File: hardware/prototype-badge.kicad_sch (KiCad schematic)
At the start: 31 parts, among them J1 GCT4105, SW1 BOOTSEL, SW2 RESET, U1 USBLC6-2SC6, U2 AMS1117-3.3, U3 W25Q32JVSS, U4 RP2040, Y1 12MHz

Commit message: started pcb
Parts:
- added C17, C19: 4.7uF, Capacitor_SMD:C_0603_1608Metric, symbol Device:C_Small
- added C18, C20, C21, C22, C23, C24, C25, C26, C28: 1uF, Capacitor_SMD:C_0603_1608Metric, symbol Device:C_Small
- added C27: 220nF, Capacitor_SMD:C_0402_1005Metric, symbol Device:C_Small
- added C29: 100nF, Capacitor_SMD:C_0402_1005Metric, symbol Device:C_Small
- added D1, D2, D3: MBR0530, Diode_SMD:D_SOD-123, symbol Diode:MBR0530
- added D4: LED_Small, LED_SMD:LED_0603_1608Metric, symbol Device:LED_Small
- added D5: D_Photo, OptoDevice:Kingbright_KPS-3227, symbol Device:D_Photo
- added J2: E-Ink, Connector_FFC-FPC:TE_2-1734839-4_1x24-1MP_P0.5mm_Horizontal, symbol Connector_Generic_MountingPin:Conn_01x24_MountingPin
- added L1: 10uH, Inductor_SMD:L_APV_ANR4018, symbol Device:L_Small
- added Q1: Si1308EDL, Package_TO_SOT_SMD:SOT-323_SC-70, symbol Transistor_FET:Si1308EDL
- added R12: 47R, Resistor_SMD:R_0603_1608Metric, symbol Device:R_Small_US
- added R13, R14: 10kR, Resistor_SMD:R_0402_1005Metric, symbol Device:R_Small_US
- added R15: 220kR, Resistor_SMD:R_0603_1608Metric, symbol Device:R_Small_US
- added R8: 1MR, Resistor_SMD:R_0603_1608Metric, symbol Device:R_Small_US
- added R9: 2.2R, Resistor_SMD:R_0603_1608Metric, symbol Device:R_Small_US
- added SW3: User1, Button_Switch_SMD:SW_Tactile_SPST_NO_Straight_CK_PTS636Sx25SMTRLFS, symbol Switch:SW_Push
- added SW4: User2, Button_Switch_SMD:SW_Tactile_SPST_NO_Straight_CK_PTS636Sx25SMTRLFS, symbol Switch:SW_Push
- added SW5: User3, Button_Switch_SMD:SW_Tactile_SPST_NO_Straight_CK_PTS636Sx25SMTRLFS, symbol Switch:SW_Push
- added SW6: User4, Button_Switch_SMD:SW_Tactile_SPST_NO_Straight_CK_PTS636Sx25SMTRLFS, symbol Switch:SW_Push
- added SW7: LIGHTPROG, Button_Switch_SMD:SW_Tactile_SPST_NO_Straight_CK_PTS636Sx25SMTRLFS, symbol Switch:SW_Push
- added U5: NT3H2111-2211, footprints:NT3H2111W0FHKH, symbol prototype-badge:NT3H2111_2211
- added U6: LMV321, Package_TO_SOT_SMD:SOT-23-5, symbol Amplifier_Operational:LMV321
- C10, C11, C12, C13, C14, C15, C16, C3, C6, C7: footprint (none) -> Capacitor_SMD:C_0402_1005Metric; LCSC (none) -> C1525
- C4, C5: value ? -> 12pF; footprint (none) -> Capacitor_SMD:C_0402_1005Metric; LCSC (none) -> C1547
- C8, C9: footprint (none) -> Capacitor_SMD:C_0603_1608Metric; LCSC (none) -> C15849
- R1, R2: footprint (none) -> Resistor_SMD:R_0402_1005Metric; LCSC (none) -> C25905
- R3: footprint (none) -> Resistor_SMD:R_0402_1005Metric; LCSC (none) -> C25744
- R4, R5: footprint (none) -> Resistor_SMD:R_0402_1005Metric; LCSC (none) -> C274349
- R6, R7: footprint (none) -> Resistor_SMD:R_0402_1005Metric; LCSC (none) -> C11702
- SW1, SW2: footprint (none) -> Button_Switch_SMD:SW_Tactile_SPST_NO_Straight_CK_PTS636Sx25SMTRLFS; LCSC (none) -> C318938
- U3: LCSC (none) -> C97521
- U4: LCSC (none) -> C2040
- Y1: LCSC (none) -> C37635368
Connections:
- net +3.3V: now also C19.1, C20.2, C28.1, J2.10 (Pin_10), J2.9 (Pin_9), L1.1, R13.1, U5.6 (VDD), U6.5 (V+)
- net Earth: now also C18.2, C19.2, C20.1, C21.1, C22.1, C23.1, C24.1, C25.1, C26.2, C27.2, C28.2, C29.1, D2.1 (K), D4.1 (K), D5.2 (A), J2.17 (Pin_17), J2.8 (Pin_8), J2.MP (MountPin), R14.2, R8.1, R9.2, SW3.2, SW4.2, SW5.2, SW6.2, SW7.2, U5.2 (VSS), U6.2 (V-)
- net GPIO13: now also SW7.1
- net GPIO14: now also SW3.1
- net GPIO15: now also SW4.1
- net GPIO16: now also SW5.1
- net GPIO17: now also SW6.1
- net GPIO0 renamed I2C_SDA
- net I2C_SDA: now also U5.5 (SDA)
- net GPIO1 renamed I2C_SCL
- net I2C_SCL: now also U5.3 (SCL)
- net GPIO18 renamed SPI_CLK
- net SPI_CLK: now also J2.12 (Pin_12)
- net GPIO19 renamed SPI_MOSI
- net SPI_MOSI: now also J2.11 (Pin_11)
- net GPIO24 renamed DISP_CS
- net DISP_CS: now also J2.13 (Pin_13)
- net GPIO25 renamed DISP_DC
- net DISP_DC: now also J2.14 (Pin_14)
- net GPIO26_ADC0 renamed DISP_RST
- net DISP_RST: now also J2.15 (Pin_15)
- net GPIO27_ADC1 renamed DISP_BUSY
- net DISP_BUSY: now also J2.16 (Pin_16)
- net GPIO28_ADC2 renamed GPIO28_ADC2_LDR
- net GPIO28_ADC2_LDR: now also R15.1, U6.4
- new net: C26.1, J2.1 (Pin_1)
- new net: C29.2, R13.2, R14.1, U6.1 (+)
- new net: D5.1 (K), R15.2, U6.3 (-)
- new net: C27.1, R12.1, U5.7 (VOUT)
- new net: D4.2 (A), R12.2
- new net: C17.2, D3.2 (A), L1.2, Q1.3 (D)
- new net: C23.2, J2.5 (Pin_5)
- new net: U5.1 (LA), U5.8 (LB)
- new net: C17.1, D1.1 (K), D2.2 (A)
- new net: C21.2, J2.20 (Pin_20)
- new net: C24.2, J2.3 (Pin_3)
- new net: C22.2, J2.7 (Pin_7)
- new net DISP_GDR: J2.23 (Pin_23), Q1.1 (G), R8.2
- new net DISP_PREVGH: C18.1, D3.1 (K), J2.4 (Pin_4)
- new net DISP_PREVGL: C25.2, D1.2 (A), J2.2 (Pin_2)
- new net DISP_RESE: J2.22 (Pin_22), Q1.2 (S), R9.1
- no-connect marks 5 -> 11
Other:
- note added: "---FLIPPED PINS FOR TOP MOUNT---"
- note added: "E-Ink Display - 2.9""
- note added: "NFC Tag"
- note added: "Photodiode"
- note added: "Press to activate light programming"
- note added: "RP2040 MCU"
- note added: "USB Input"
- note added: "User-Facing Buttons"
- note added: "config over light?"
- note added: "overcomplicated TIA circuit"
- title: (none) -> Prototype PCB Badges
- moved on the sheet: C1, C10, C11, C12, C13, C14, C15, C16, C2, C3, C4, C5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

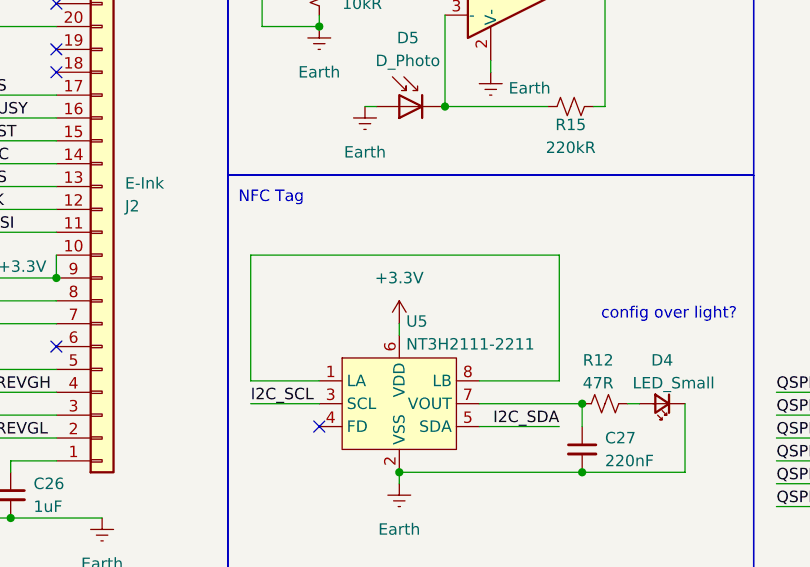
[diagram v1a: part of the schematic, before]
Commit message: 90% done with pcb, need to add dev pins
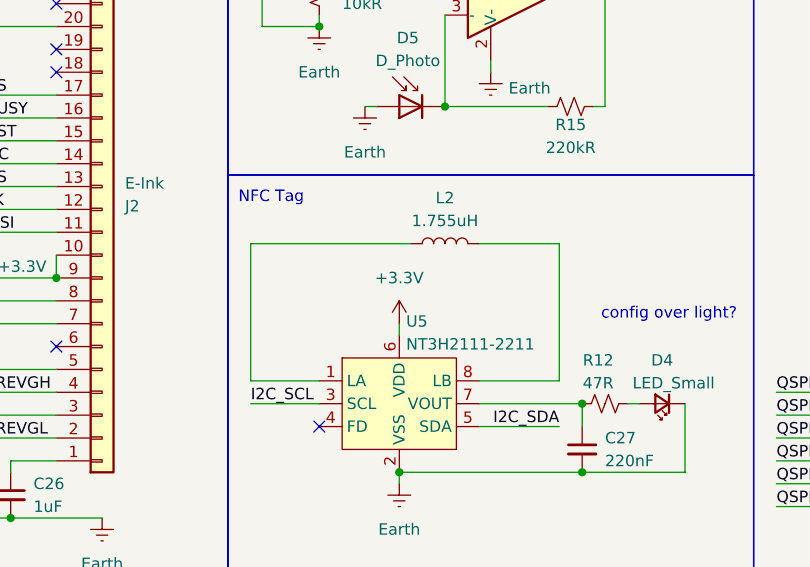
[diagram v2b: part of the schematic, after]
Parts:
- added L2: 1.755uH, footprints:nfc-coil-2, symbol Device:L
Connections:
- net at U5.1 (LA): now also L2.1; no longer U5.8 (LB)
- new net: L2.2, U5.8 (LB)
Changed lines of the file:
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@@
 	(wire
 		(pts
+			(xy 148.59 120.65) (xy 148.59 135.89)
+		)
+		(stroke
+			(width 0)
+			(type default)
+		)
+	)
+	(wire
+		(pts
 			(xy 226.06 156.21) (xy 224.79 156.21)
 		)
@@
 	(wire
 		(pts
-			(xy 148.59 135.89) (xy 148.59 121.92)
+			(xy 193.04 130.81) (xy 193.04 132.08)
 		)
 		(stroke
@@
 	(wire
 		(pts
-			(xy 193.04 130.81) (xy 193.04 132.08)
+			(xy 182.88 50.8) (xy 191.77 50.8)
 		)
 		(stroke
@@
 	(wire
 		(pts
-			(xy 182.88 50.8) (xy 191.77 50.8)
+			(xy 148.59 120.65) (xy 139.7 120.65)
 		)
 		(stroke
@@
 	(wire
 		(pts
-			(xy 114.3 121.92) (xy 114.3 135.89)
+			(xy 44.45 40.64) (xy 44.45 43.18)
 		)
 		(stroke
@@
 	(wire
 		(pts
-			(xy 44.45 40.64) (xy 44.45 43.18)
+			(xy 193.04 158.75) (xy 193.04 157.48)
 		)
 		(stroke
@@
 	(wire
 		(pts
-			(xy 193.04 158.75) (xy 193.04 157.48)
+			(xy 148.59 35.56) (xy 148.59 45.72)
 		)
 		(stroke
@@
 	(wire
 		(pts
-			(xy 148.59 35.56) (xy 148.59 45.72)
+			(xy 191.77 36.83) (xy 191.77 38.1)
 		)
 		(stroke
@@
 	(wire
 		(pts
-			(xy 191.77 36.83) (xy 191.77 38.1)
+			(xy 248.92 116.84) (xy 270.51 116.84)
 		)
 		(stroke
@@
 	(wire
 		(pts
-			(xy 248.92 116.84) (xy 270.51 116.84)
+			(xy 232.41 149.86) (xy 229.87 149.86)
 		)
 		(stroke
@@
 	(wire
 		(pts
-			(xy 232.41 149.86) (xy 229.87 149.86)
+			(xy 114.3 120.65) (xy 114.3 135.89)
 		)
 		(stroke
@@
 	(wire
 		(pts
-			(xy 191.77 43.18) (xy 198.12 43.18)
+			(xy 132.08 120.65) (xy 114.3 120.65)
 		)
 		(stroke
@@
 	(wire
 		(pts
-			(xy 39.37 142.24) (xy 39.37 130.81)
+			(xy 191.77 43.18) (xy 198.12 43.18)
 		)
 		(stroke
@@
 	(wire
 		(pts
-			(xy 80.01 88.9) (xy 92.71 88.9)
+			(xy 39.37 142.24) (xy 39.37 130.81)
 		)
 		(stroke
@@
 	(wire
 		(pts
-			(xy 130.81 147.32) (xy 130.81 146.05)
+			(xy 80.01 88.9) (xy 92.71 88.9)
 		)
 		(stroke
@@
 	(wire
 		(pts
-			(xy 266.7 53.34) (xy 248.92 53.34)
+			(xy 130.81 147.32) (xy 130.81 146.05)
 		)
 		(stroke
@@
 	(wire
 		(pts
-			(xy 80.01 111.76) (xy 92.71 111.76)
+			(xy 266.7 53.34) (xy 248.92 53.34)
 		)
 		(stroke
@@
 	(wire
 		(pts
-			(xy 148.59 121.92) (xy 114.3 121.92)
+			(xy 80.01 111.76) (xy 92.71 111.76)
 		)
 		(stroke
@@
 			"hBBCCCGEEEIIIYQQQgghhBBCCCGEEEIIIYQQQgghhBBCCCGEEEIIIYQQQgghhBBCCCGEEEIIIYQQ"
 			"QgghhBBCCCGEEEIIIYQQQgghhBBCCCGEEEIIIYQQQgghhBBCCCGEEEIIIYQQQhai/w/KaxpFstuM"
-			"6gAAAABJRU5ErkJggg=="
+			"6gAAAABJRU5ErkJgggAAAAAAAAAAAAAAAAAAAAAAAAAAAAAAAAAAAAAAAAAAAAAAAAAAAAAAAAAA"
+			"AAAAAAAAAAAAAAAAAAAAAAAAAAAAAAAAAAAAAAAAAAAAAAAAAAAAAAAAAAAAAAAAAAAAAAAAAAAA"
+			"AAAAAAAAAAAAAAAAAAAAAAAAAAAAAAAAAAAAAAAAAAAAAAAAAAAAAAAAAAAAAAAAAAAAAAAAAAAA"
+			"AAAAAAAAAAAAAAAAAAAAAAAAAAAAAAAAAAAAAAAAAAAAAAAAAAAAAAAAAAAAAAAAAAAAAAAAAAAA"
+			"AAAAAAAAAAAAAAAAAAAAAAAAAAAAAAAAAAAAAAAAAAAAAAAAAAAAAAAAAAAAAAAAAAAAAAAAAAAA"
+			"AAAAAAAAAAAAAAAAAAAAAAAAAAAAAAAAAAAAAAAAAAAAAAAAAAAAAAAAAAAAAAAAAAAAAAAAAAAA"
+			"AAAAAAAAAAAAAAAAAAAAAAAAAAAAAAAAAAAAAAAAAAAAAAAAAAAAAAAAAAAAAAAAAAAAAAAAAAAA"
+			"AAAAAAAAAAAAAAAAAAAAAAAAAAAAAAAAAAAAAAAAAAAAAAAAAAAAAAAAAAAAAAAAAAAAAAAAAAAA"
+			"AAAAAAAAAAAAAAAAAAAAAAAAAAAAAAAAAAAAAAAAAAAAAAAAAAAAAAAAAAAAAAAAAAAAAAAAAAAA"
+			"AAAAAAAAAAAAAAAAAAAAAAAAAAAAAAAAAAAAAAAAAAAAAAAAAAAAAAAAAAAAAAAAAAAAAAAAAAAA"
+			"AAAAAAAAAAAAAAAAAAAAAAAAAAAAAAAAAAAAAAAAAAAAAAAAAAAAAAAAAAAAAAAAAAAAAAAAAAAA"
+			"AAAAAAAAAAAAAAAAAAAAAAAAAAAAAAAAAAAAAAAAAAAAAAAAAAAAAAAAAAAAAAAAAAAAAAAAAAAA"
+			"AAAAAAAAAAAAAAAAAAAAAAAAAAAAAAAAAAAAAAAAAAAAAAAAAAAAAAAAAAAAAAAAAAAAAAAAAAAA"
+			"AAAAAAAAAAAAAAAAAAAAAAAAAAAAAAAAAAAAAAAAAAAAAAAAAAAAAAAAAAAAAAAAAAAAAAAAAAAA"
+			"AAAAAAAAAAAAAAAAAAAAAAAAAAAAAAAAAAAAAAAAAAAAAAAAAAAAAAAAAAAAAAAAAAAAAAAAAAAA"
+			"AAAAAAAAAAAAAAAAAAAAAAAAAAAAAAAAAAAAAAAAAAAAAAAAAAAAAAAAAAAAAAAAAAAAAAAAAAAA"
+			"AAAAAAAAAAAAAAAAAAAAAAAAAAAAAAAAAAAAAAAAAAAAAAAAAAAAAAAAAAAAAAAAAAAAAAAAAAAA"
+			"AAAAAAAAAAAAAAAAAAAAAAAAAAAAAAAAAAAAAAAAAAAAAAAAAAAAAAAAAAAAAAAAAAAAAAAAAAAA"
+			"AAAAAAAAAAAAAAAAAAAAAAAAAAAAAAAAAAAAAAAAAAAAAAAAAAAAAAAAAAAAAAAAAAAAAAAAAAAA"
+			"AAAAAAAAAAAAAAAAAAAAAAAAAAAAAAAAAAAAAAAAAAAAAAAAAAAAAAAAAAAAAAAAAAAAAAAAAAAA"
+			"AAAAAAAAAAAAAAAAAAAAAAAAAAAAAAAAAAAAAAAAAAAAAAAAAAAAAAAAAAAAAAAAAAAAAAAAAAAA"
+			"AAAAAAAAAAAAAAAAAAAAAAAAAAAAAAAAAAAAAAAAAAAAAAAAAAAAAAAAAAAAAAAAAAAAAAAAAAAA"
+			"AAAAAAAAAAAAAAAAAAAAAAAAAAAAAAAAAAAAAAAAAAAAAAAAAAAAAAAAAAAAAAAAAAAAAAAAAAAA"
+			"AAAAAAAAAAAAAAAAAAAAAAAAAAAAAAAAAAAAAAAAAAAAAAAAAAAAAAAAAAAAAAAAAAAAAAAAAAAA"
+			"AAAAAAAAAAAAAAAAAAAAAAAAAAAAAAAAAAAAAAAAAAAAAAAAAAAAAAAAAAAAAAAAAAAAAAAAAAAA"
+			"AAAAAAAAAAAAAAAAAAAAAAAAAAAAAAAAAAAAAAAAAAAAAAAAAAAAAAAAAAAAAAAAAAAAAAAAAAAA"
+			"AAAAAAAAAAAAAAAAAAAAAAAAAAAAAAAAAAAAAAAAAAAAAAAAAAAAAAAAAAAAAAAAAAAAAAAAAAAA"
+			"AAAAAAAAAAAAAAAAAAAAAAAAAAAAAAAAAAAAAAAAAAAAAAAAAAAAAAAAAAAAAAAAAAAAAAAAAAAA"
+			"AAAAAAAAAAAAAAAAAAAAAAAAAAAAAAAAAAAAAAAAAAAAAAAAAAAAAAAAAAAAAAAAAAAAAAAAAAAA"
+			"AAAAAAAAAAAAAAAAAAAAAAAAAAAAAAAAAAAAAAAAAAAAAAAAAAAAAAAAAAAAAAAAAAAAAAAAAAAA"
+			"AAAAAAAAAAAAAAAAAAAAAAAAAAAAAAAAAAAAAAAAAAAAAAAAAAAAAAAAAAAAAAAAAAAAAAAAAAAA"
+			"AAAAAAAAAAAAAAAAAAAAAAAAAAAAAAAAAAAAAAAAAAAAAAAAAAAAAAAAAAAAAAAAAAAAAAAAAAAA"
+			"AAAAAAAAAAAAAAAAAAAAAAAAAAAAAAAAAAAAAAAAAAAAAAAAAAAAAAAAAAAAAAAAAAAAAAAAAAAA"
+			"AAAAAAAAAAAAAAAAAAAAAAAAAAAAAAAAAAAAAAAAAAAAAAAAAAAAAAAAAAAAAAAAAAAAAAAAAAAA"
+			"AAAAAAAAAAAAAAAAAAAAAAAAAAAAAAAAAAAAAAAAAAAAAAAAAAAAAAAAAAAAAAAAAAAAAAAAAAAA"
+			"AAAAAAAAAAAAAAAAAAAAAAAAAAAAAAAAAAAAAAAAAAAAAAAAAAAAAAAAAAAAAAAAAAAAAAAAAAAA"
+			"AAAAAAAAAAAAAAAAAA=="
 		)
 	)
@@
 			"K8ZsyVreCyWJuaoBAAAAAAAAAAAAAAAAAAAAAAAAAAAAAAAAAAAAAAAAAAAAAAAAAAAAAAAAAAAA"
 			"AAAAAAAAAAAAAAAAAAAAAAAAAAAAAAAAAAAAAAAAAAAAAAAAAAAAAAAAAAAAAACwOv0fB0wq9b7e"
-			"qgAAAAAASUVORK5CYII="
+			"qgAAAAAASUVORK5CYIIAAAAAAAAAAAAAAAAAAAAAAAAAAAAAAAAAAAAAAAAAAAAAAAAAAAAAAAAA"
+			"AAAAAAAAAAAAAAAAAAAAAAAAAAAAAAAAAAAAAAAAAAAAAAAAAAAAAAAAAAAAAAAAAAAAAAAAAAAA"
+			"AAAAAAAAAAAAAAAAAAAAAAAAAAAAAAAAAAAAAAAAAAAAAAAAAAAAAAAAAAAAAAAAAAAAAAAAAAAA"
+			"AAAAAAAAAAAAAAAAAAAAAAAAAAAAAAAAAAAAAAAAAAAAAAAAAAAAAAAAAAAAAAAAAAAAAAAAAAAA"
+			"AAAAAAAAAAAAAAAAAAAAAAAAAAAAAAAAAAAAAAAAAAAAAAAAAAAAAAAAAAAAAAAAAAAAAAAAAAAA"
+			"AAAAAAAAAAAAAAAAAAAAAAAAAAAAAAAAAAAAAAAAAAAAAAAAAAAAAAAAAAAAAAAAAAAAAAAAAAAA"
+			"AAAAAAAAAAAAAAAAAAAAAAAAAAAAAAAAAAAAAAAAAAAAAAAAAAAAAAAAAAAAAAAAAAAAAAAAAAAA"
+			"AAAAAAAAAAAAAAAAAAAAAAAAAAAAAAAAAAAAAAAAAAAAAAAAAAAAAAAAAAAAAAAAAAAAAAAAAAAA"
+			"AAAAAAAAAAAAAAAAAAAAAAAAAAAAAAAAAAAAAAAAAAAAAAAAAAAAAAAAAAAAAAAAAAAAAAAAAAAA"
+			"AAAAAAAAAAAAAAAAAAAAAAAAAAAAAAAAAAAAAAAAAAAAAAAAAAAAAAAAAAAAAAAAAAAAAAAAAAAA"
+			"AAAAAAAAAAAAAAAAAAAAAAAAAAAAAAAAAAAAAAAAAAAAAAAAAAAAAAAAAAAAAAAAAAAAAAAAAAAA"
+			"AAAAAAAAAAAAAAAAAAAAAAAAAAAAAAAAAAAAAAAAAAAAAAAAAAAAAAAAAAAAAAAAAAAAAAAAAAAA"
+			"AAAAAAAAAAAAAAAAAAAAAAAAAAAAAAAAAAAAAAAAAAAAAAAAAAAAAAAAAAAAAAAAAAAAAAAAAAAA"
+			"AAAAAAAAAAAAAAAAAAAAAAAAAAAAAAAAAAAAAAAAAAAAAAAAAAAAAAAAAAAAAAAAAAAAAAAAAAAA"
+			"AAAAAAAAAAAAAAAAAAAAAAAAAAAAAAAAAAAAAAAAAAAAAAAAAAAAAAAAAAAAAAAAAAAAAAAAAAAA"
+			"AAAAAAAAAAAAAAAAAAAAAAAAAAAAAAAAAAAAAAAAAAAAAAAAAAAAAAAAAAAAAAAAAAAAAAAAAAAA"
+			"AAAAAAAAAAAAAAAAAAAAAAAAAAAAAAAAAAAAAAAAAAAAAAAAAAAAAAAAAAAAAAAAAAAAAAAAAAAA"
+			"AAAAAAAAAAAAAAAAAAAAAAAAAAAAAAAAAAAAAAAAAAAAAAAAAAAAAAAAAAAAAAAAAAAAAAAAAAAA"
+			"AAAAAAAAAAAAAAAAAAAAAAAAAAAAAAAAAAAAAAAAAAAAAAAAAAAAAAAAAAAAAAAAAAAAAAAAAAAA"
+			"AAAAAAAAAAAAAAAAAAAAAAAAAAAAAAAAAAAAAAAAAAAAAAAAAAAAAAAAAAAAAAAAAAAAAAAAAAAA"
+			"AAAAAAAAAAAAAAAAAAAAAAAAAAAAAAAAAAAAAAAAAAAAAAAAAAAAAAAAAAAAAAAAAAAAAAAAAAAA"
+			"AAAAAAAAAAAAAAAAAAAAAAAAAAAAAAAAAAAAAAAAAAAAAAAAAAAAAAAAAAAAAAAAAAAAAAAAAAAA"
+			"AAAAAAAAAAAAAAAAAAAAAAAAAAAAAAAAAAAAAAAAAAAAAAAAAAAAAAAAAAAAAAAAAAAAAAAAAAAA"
+			"AAAAAAAAAAAAAAAAAAAAAAAAAAAAAAAAAAAAAAAAAAAAAAAAAAAAAAAAAAAAAAAAAAAAAAAAAAAA"
+			"AAAAAAAAAAAAAAAAAAAAAAAAAAAAAAAAAAAAAAAAAAAAAAAAAAAAAAAAAAAAAAAAAAAAAAAAAAAA"
+			"AAAAAAAAAAAAAAAAAAAAAAAAAAAAAAAAAAAAAAAAAAAAAAAAAAAAAAAAAAAAAAAAAAAAAAAAAAAA"
+			"AAAAAAAAAAAAAAAAAAAAAAAAAAAAAAAAAAAAAAAAAAAAAAAAAAAAAAAAAAAAAAAAAAAAAAAAAAAA"
+			"AAAAAAAAAAAAAAAAAAAAAAAAAAAAAAAAAAAAAAAAAAAAAAAAAAAAAAAAAAAAAAAAAAAAAAAAAAAA"
+			"AAAAAAAAAAAAAAAAAAAAAAAAAAAAAAAAAAAAAAAAAAAAAAAAAAAAAAAAAAAAAAAAAAAAAAAAAAAA"
+			"AAAAAAAAAAAAAAAAAAAAAAAAAAAAAAAAAAAAAAAAAAAAAAAAAAAAAAAAAAAAAAAAAAAAAAAAAAAA"
+			"AAAAAAAAAAAAAAAAAAAAAAAAAAAAAAAAAAAAAAAAAAAAAAAAAAAAAAAAAAAAAAAAAAAAAAAAAAAA"
+			"AAAAAAAAAAAAAAAAAAAAAAAAAAAAAAAAAAAAAAAAAAAAAAAAAAAAAAAAAAAAAAAAAAAAAAAAAAAA"
+			"AAAAAAAAAAAAAAAAAAAAAAAAAAAAAAAAAAAAAAAAAAAAAAAAAAAAAAAAAAAAAAAAAAAAAAAAAAAA"
+			"AAAAAAAAAAAAAAAAAAAAAAAAAAAAAAAAAAAAAAAAAAAAAAAAAAAAAAAAAAAAAAAAAAAAAAAAAAAA"
+			"AAAAAAAAAAAAAAAAAAAAAAAAAAAAAAAAAAAAAAAAAAAAAAAAAAAAAAAAAAAAAAAAAAAAAAAAAAAA"
+			"AAAAAAAAAAAAAAAAAAAAAAAAAAAAAAAAAAAAAAAAAAAAAAAAAAAAAAAAAAAAAAAAAAAAAAAAAAAA"
+			"AAAAAAAAAAAAAAAAAA=="
 		)
 	)
@@
 					(unit 1)
 				)
+			)
+		)
+	)
+	(symbol
+		(lib_id "Device:L")
+		(at 135.89 120.65 90)
+		(unit 1)
+		(exclude_from_sim no)
+		(in_bom yes)
+		(on_board yes)
+		(dnp no)
+		(fields_autoplaced yes)
+		(property "Reference" "L2"
+			(at 135.89 115.57 90)
+			(effects
+				(font
+					(size 1.27 1.27)
+				)
+			)
+		)
+		(property "Value" "1.755uH"
+			(at 135.89 118.11 90)
+			(effects
+				(font
+					(size 1.27 1.27)
+				)
+			)
+		)
+		(property "Footprint" "footprints:nfc-coil-2"
+			(at 135.89 120.65 0)
+			(effects
+				(font
+					(size 1.27 1.27)
+				)
+				(hide yes)
+			)
+		)
+		(property "Datasheet" "~"
+			(at 135.89 120.65 0)
+			(effects
+				(font
+					(size 1.27 1.27)
+				)
+				(hide yes)
+			)
+		)
+		(property "Description" "Inductor"
+			(at 135.89 120.65 0)
+			(effects
+				(font
+					(size 1.27 1.27)
+				)
+				(hide yes)
+			)
+		)
+		(pin "1"
+		)
+		(pin "2"
+		)
+		(instances
+			(project ""
+				(path "/77891dc8-24bc-465d-8132-75a6c64b6b1f"
+					(reference "L2")
+					(unit 1)
+				)

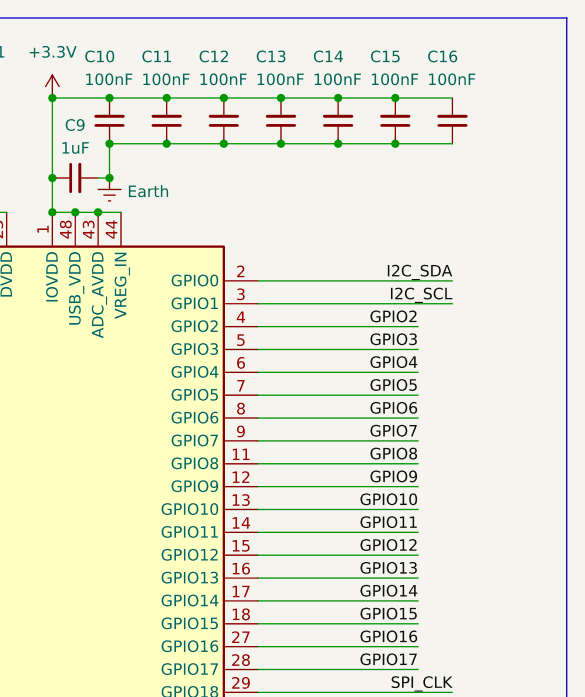
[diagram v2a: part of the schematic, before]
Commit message: added gpio pins - next up: finalize outline (add fpc connector + corners), add art
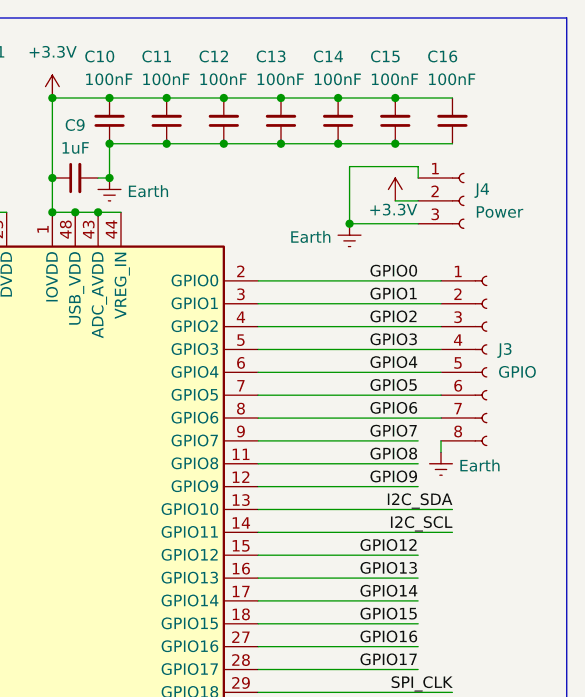
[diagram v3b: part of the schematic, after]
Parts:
- added J3: GPIO, Connector_PinSocket_2.54mm:PinSocket_1x08_P2.54mm_Vertical, symbol Connector:Conn_01x08_Socket
- added J4: Power, Connector_PinSocket_2.54mm:PinSocket_1x03_P2.54mm_Vertical, symbol Connector:Conn_01x03_Socket
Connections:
- net GPIO10 is gone; now on net I2C_SDA: U4.13 (GPIO10)
- net GPIO11 is gone; now on net I2C_SCL: U4.14 (GPIO11)
- net +3.3V: now also J4.2 (Pin_2)
- net Earth: now also J3.8 (Pin_8), J4.1 (Pin_1), J4.3 (Pin_3)
- net GPIO2: now also J3.3 (Pin_3)
- net GPIO3: now also J3.4 (Pin_4)
- net GPIO4: now also J3.5 (Pin_5)
- net GPIO5: now also J3.6 (Pin_6)
- net GPIO6: now also J3.7 (Pin_7)
- net I2C_SCL: no longer U4.3 (GPIO1)
- net I2C_SDA: no longer U4.2 (GPIO0)
- new net GPIO0: J3.1 (Pin_1), U4.2 (GPIO0)
- new net GPIO1: J3.2 (Pin_2), U4.3 (GPIO1)

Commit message: v2 - new layout and reworked routing
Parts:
- removed J3: GPIO, Connector_PinSocket_2.54mm:PinSocket_1x08_P2.54mm_Vertical, symbol Connector:Conn_01x08_Socket
- removed J4: Power, Connector_PinSocket_2.54mm:PinSocket_1x03_P2.54mm_Vertical, symbol Connector:Conn_01x03_Socket
- added J3: Conn_01x11_Socket, Connector_PinSocket_2.54mm:PinSocket_1x11_P2.54mm_Vertical, symbol Connector:Conn_01x11_Socket
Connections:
- net +3.3V: now also J3.2 (Pin_2)
- net Earth: now also J3.1 (Pin_1), J3.11 (Pin_11), J3.3 (Pin_3)
- net GPIO0: now also J3.4 (Pin_4)
- net GPIO1: now also J3.5 (Pin_5)
- net GPIO2: now also J3.6 (Pin_6)
- net GPIO3: now also J3.7 (Pin_7)
- net GPIO4: now also J3.8 (Pin_8)
- net GPIO5: now also J3.9 (Pin_9)
- net GPIO6: now also J3.10 (Pin_10)
